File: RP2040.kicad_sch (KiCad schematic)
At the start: 1 part, among them U1 RP2040

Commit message: more rp2040 work
-BMS updates
- rp2040 updates
- add hardware design docs
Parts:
- added C1, C10, C11, C12, C13, C14, C15, C18, C19, C9: 10µF, symbol Device:C_Small
- added C16, C17: 1µF, symbol Device:C_Small
- added R5, R6: 27.4Ω, symbol Device:R_Small
- U1: Hardware Design Docs (none) -> https://datasheets.raspberrypi.com/rp2040/hardware-design-w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
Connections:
- net +3v3-SYS: now also C1.1, C10.1, C11.1, C12.1, C13.1, C14.1, C15.1, C16.1, C9.1
- net GND: now also C1.2, C10.2, C11.2, C12.2, C13.2, C14.2, C15.2, C16.2, C17.1, C18.2, C19.2, C9.2
- net +1V1: now reaches U1.23 (DVDD), U1.50 (DVDD)
- net +1V1: now also U1.45 (VREG_VOUT), C17.2, C18.1, C19.1
- net at U1.46 (USB_DM): now also R6.1
- net at U1.47 (USB_DP): now also R5.2
- net QSPI_SD3: now reaches U1.51 (QSPI_SD3)
- net QSPI_SCLK: now reaches U1.52 (QSPI_SCLK)
- net QSPI_SD0: now reaches U1.53 (QSPI_SD0)
- net QSPI_SD2: now reaches U1.54 (QSPI_SD2)
- net QSPI_SD1: now reaches U1.55 (QSPI_SD1)
- net QSPI_SS: now reaches U1.56 (QSPI_SS)
- net MB_SCL renamed SCL2
- net MB_SDA renamed SDA2
- net SYS_SCL renamed SCL1
- net SYS_SDA renamed SDA1
- new net USB_DM: R6.2
- new net USB_DP: R5.1
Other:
- note added: "1µF close to VREG_IN"
- note added: "1µF close to VREG_VOUT"
- note added: "27.4Ω close to D+/D-"
- moved on the sheet: U1

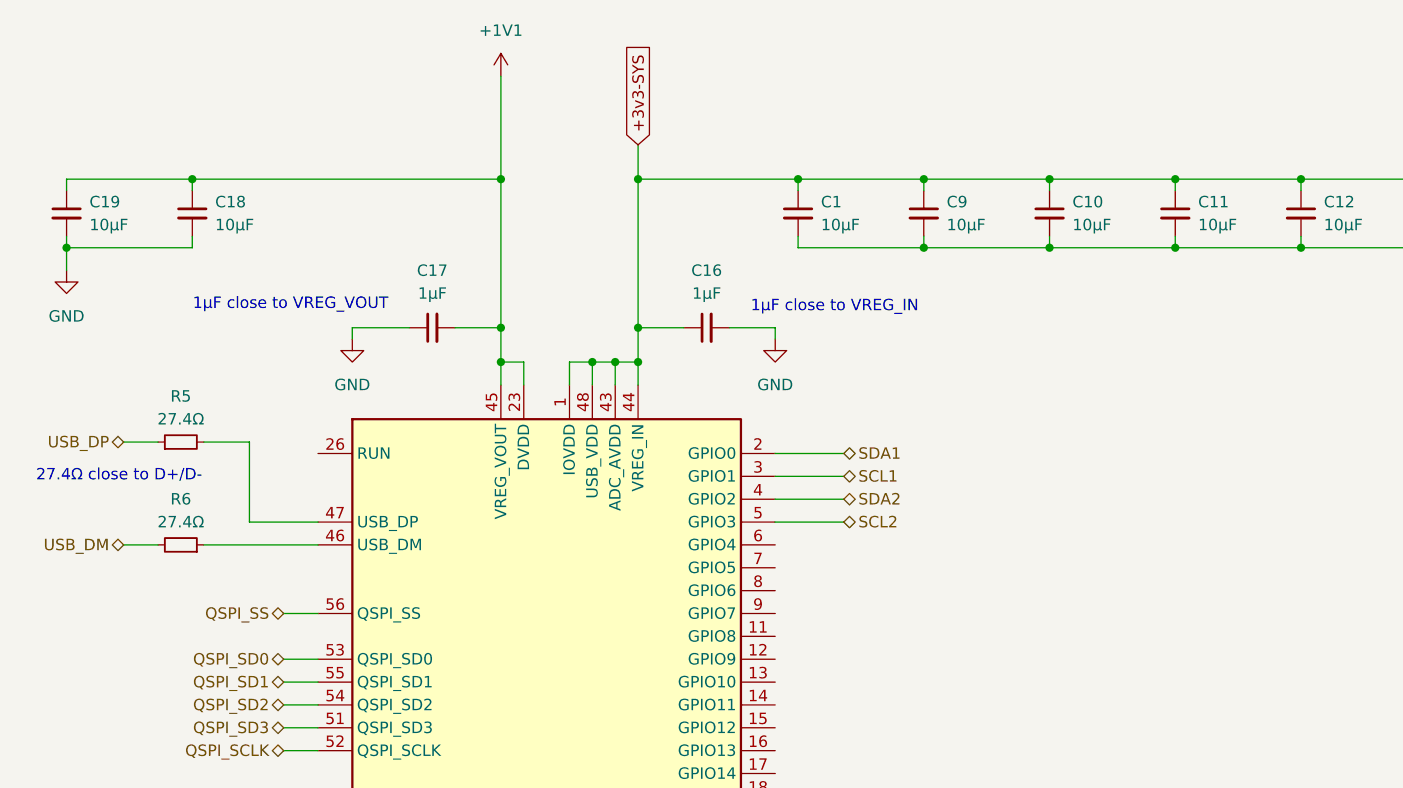
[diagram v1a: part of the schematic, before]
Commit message: BMS updates
- BMS mostly done
- all BMS pins connected to RP2040
- Re-did Minibadge pinouts
- Connected RP2040 to USB Switch
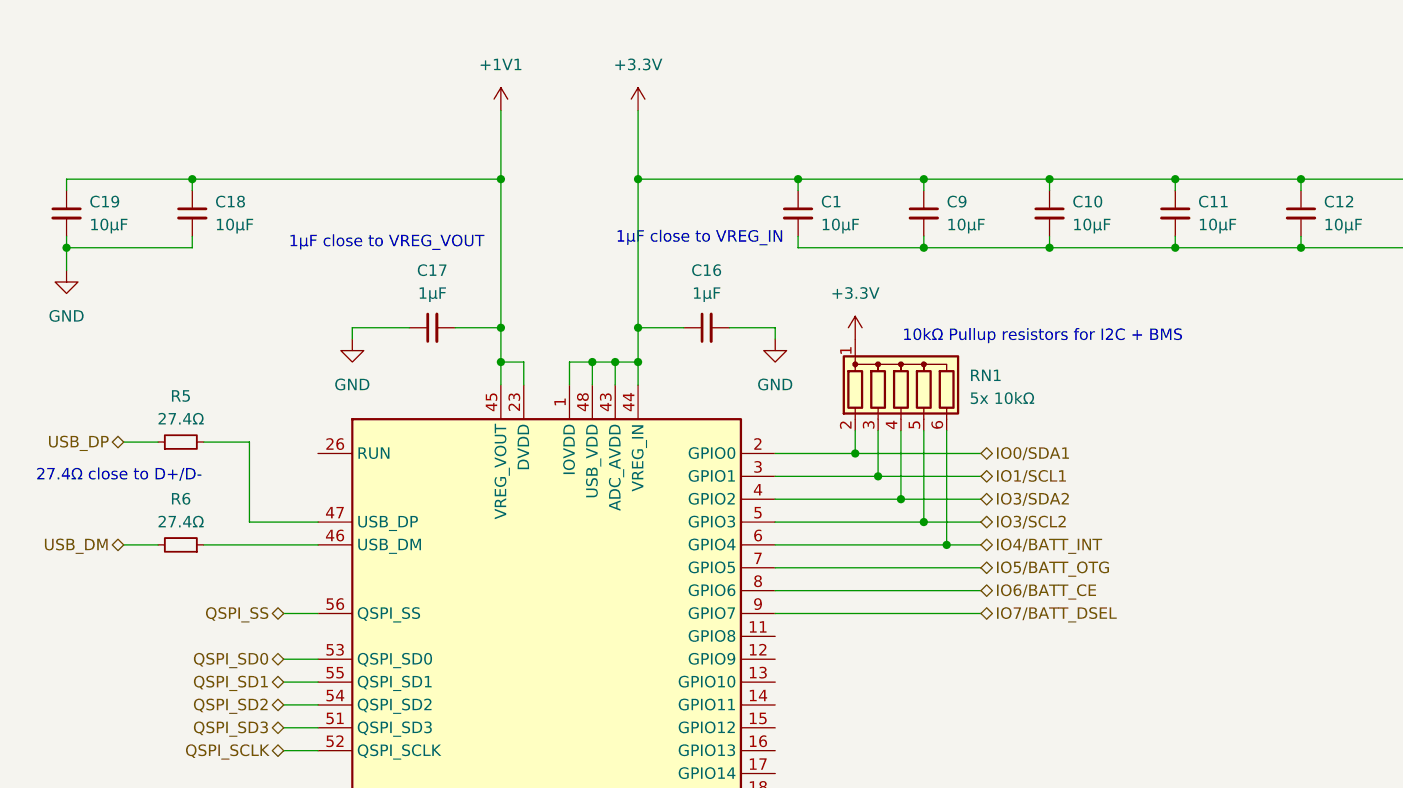
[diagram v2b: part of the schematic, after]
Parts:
- added RN1: 5x 10kΩ, Resistor_THT:R_Array_SIP6, symbol Device:R_Network05
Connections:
- net IO4/BATT_INT: now reaches U1.6 (GPIO4)
- net IO4/BATT_INT: now also RN1.6 (R5)
- net IO5/BATT_OTG: now reaches U1.7 (GPIO5)
- net IO6/BATT_CE: now reaches U1.8 (GPIO6)
- net IO7/BATT_DSEL: now reaches U1.9 (GPIO7)
- net +3v3-SYS renamed +3.3V
- net +3.3V: now also RN1.1 (common)
- net SCL1 renamed IO1/SCL1
- net IO1/SCL1: now also RN1.3 (R2)
- net SCL2 renamed IO3/SCL2
- net IO3/SCL2: now also RN1.5 (R4)
- net SDA1 renamed IO0/SDA1
- net IO0/SDA1: now also RN1.2 (R1)
- net SDA2 renamed IO3/SDA2
- net IO3/SDA2: now also RN1.4 (R3)
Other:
- note added: "10kΩ Pullup resistors for I2C + BMS"
- company: (none) -> Pips Engineering
- title: (none) -> RP2040 MCU

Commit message: cleanup
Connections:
- net IO8/USB_SW_DISABLE: now reaches U1.11 (GPIO8)
- net IO7/BATT_DSEL renamed IO7/USB_SW_DSEL
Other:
- moved on the sheet: RN1
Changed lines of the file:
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@@
 	)
 	(junction
-		(at 140.97 72.39)
-		(diameter 0)
-		(color 0 0 0 0)
-	)
-	(junction
-		(at 151.13 82.55)
+		(at 142.24 72.39)
 		(diameter 0)
 		(color 0 0 0 0)
@@
 	)
 	(junction
-		(at 143.51 74.93)
-		(diameter 0)
-		(color 0 0 0 0)
-	)
-	(junction
 		(at 176.53 49.53)
 		(diameter 0)
@@
 	)
 	(junction
+		(at 147.32 77.47)
+		(diameter 0)
+		(color 0 0 0 0)
+	)
+	(junction
 		(at 232.41 49.53)
 		(diameter 0)
@@
 	)
 	(junction
-		(at 146.05 77.47)
+		(at 152.4 82.55)
+		(diameter 0)
+		(color 0 0 0 0)
+	)
+	(junction
+		(at 149.86 80.01)
 		(diameter 0)
 		(color 0 0 0 0)
@@
 	)
 	(junction
+		(at 144.78 74.93)
+		(diameter 0)
+		(color 0 0 0 0)
+	)
+	(junction
 		(at 162.56 41.91)
 		(diameter 0)
@@
 	)
 	(junction
-		(at 148.59 80.01)
-		(diameter 0)
-		(color 0 0 0 0)
-	)
-	(junction
 		(at 101.6 62.23)
 		(diameter 0)
@@
 	(wire
 		(pts
-			(xy 132.08 82.55) (xy 151.13 82.55)
+			(xy 132.08 82.55) (xy 152.4 82.55)
 		)
 		(stroke
@@
 	(wire
 		(pts
-			(xy 148.59 80.01) (xy 154.94 80.01)
-		)
-		(stroke
-			(width 0)
-			(type default)
-		)
-	)
-	(wire
-		(pts
-			(xy 151.13 82.55) (xy 154.94 82.55)
-		)
-		(stroke
-			(width 0)
-			(type default)
-		)
-	)
-	(wire
-		(pts
 			(xy 232.41 41.91) (xy 218.44 41.91)
 		)
@@
 	(wire
 		(pts
-			(xy 143.51 69.85) (xy 143.51 74.93)
+			(xy 144.78 68.58) (xy 144.78 74.93)
 		)
 		(stroke
@@
 	(wire
 		(pts
+			(xy 132.08 92.71) (xy 154.94 92.71)
+		)
+		(stroke
+			(width 0)
+			(type default)
+		)
+	)
+	(wire
+		(pts
 			(xy 176.53 49.53) (xy 190.5 49.53)
 		)
@@
 	(wire
 		(pts
+			(xy 152.4 82.55) (xy 154.94 82.55)
+		)
+		(stroke
+			(width 0)
+			(type default)
+		)
+	)
+	(wire
+		(pts
 			(xy 218.44 48.26) (xy 218.44 49.53)
 		)
@@
 	(wire
 		(pts
-			(xy 146.05 69.85) (xy 146.05 77.47)
+			(xy 147.32 77.47) (xy 154.94 77.47)
+		)
+		(stroke
+			(width 0)
+			(type default)
+		)
+	)
+	(wire
+		(pts
+			(xy 149.86 80.01) (xy 154.94 80.01)
+		)
+		(stroke
+			(width 0)
+			(type default)
+		)
+	)
+	(wire
+		(pts
+			(xy 147.32 68.58) (xy 147.32 77.47)
 		)
 		(stroke
@@
 	(wire
 		(pts
-			(xy 148.59 69.85) (xy 148.59 80.01)
+			(xy 149.86 68.58) (xy 149.86 80.01)
 		)
 		(stroke
@@
 	(wire
 		(pts
-			(xy 132.08 80.01) (xy 148.59 80.01)
+			(xy 132.08 80.01) (xy 149.86 80.01)
 		)
 		(stroke
@@
 	(wire
 		(pts
-			(xy 146.05 77.47) (xy 154.94 77.47)
-		)
-		(stroke
-			(width 0)
-			(type default)
-		)
-	)
-	(wire
-		(pts
 			(xy 176.53 41.91) (xy 190.5 41.91)
 		)
@@
 	(wire
 		(pts
-			(xy 143.51 74.93) (xy 154.94 74.93)
-		)
-		(stroke
-			(width 0)
-			(type default)
-		)
-	)
-	(wire
-		(pts
 			(xy 190.5 49.53) (xy 204.47 49.53)
 		)
@@
 	(wire
 		(pts
-			(xy 132.08 74.93) (xy 143.51 74.93)
+			(xy 132.08 74.93) (xy 144.78 74.93)
 		)
 		(stroke
@@
 	(wire
 		(pts
-			(xy 132.08 77.47) (xy 146.05 77.47)
+			(xy 132.08 77.47) (xy 147.32 77.47)
 		)
 		(stroke
@@
 	(wire
 		(pts
-			(xy 140.97 72.39) (xy 154.94 72.39)
-		)
-		(stroke
-			(width 0)
-			(type default)
-		)
-	)
-	(wire
-		(pts
 			(xy 77.47 100.33) (xy 81.28 100.33)
 		)
@@
 	(wire
 		(pts
+			(xy 144.78 74.93) (xy 154.94 74.93)
+		)
+		(stroke
+			(width 0)
+			(type default)
+		)
+	)
+	(wire
+		(pts
 			(xy 101.6 62.23) (xy 101.6 64.77)
 		)
@@
 	(wire
 		(pts
-			(xy 140.97 69.85) (xy 140.97 72.39)
+			(xy 142.24 68.58) (xy 142.24 72.39)
 		)
 		(stroke
@@
 	(wire
 		(pts
-			(xy 132.08 72.39) (xy 140.97 72.39)
+			(xy 132.08 72.39) (xy 142.24 72.39)
 		)
 		(stroke
@@
 	(wire
 		(pts
-			(xy 151.13 69.85) (xy 151.13 82.55)
+			(xy 152.4 68.58) (xy 152.4 82.55)
 		)
 		(stroke
@@
 		(pts
 			(xy 116.84 62.23) (xy 116.84 64.77)
+		)
+		(stroke
+			(width 0)
+			(type default)
+		)
+	)
+	(wire
+		(pts
+			(xy 142.24 72.39) (xy 154.94 72.39)
 		)
 		(stroke
@@
 	(text "10kΩ Pullup resistors for I2C + BMS"
 		(exclude_from_sim no)
-		(at 161.798 59.436 0)
+		(at 163.322 58.166 0)
 		(effects
 			(font
@@
 	(text "1µF close to VREG_IN"
 		(exclude_from_sim no)
-		(at 123.698 48.514 0)
+		(at 122.682 49.022 0)
 		(effects
 			(font
@@
 		)
 	)
-	(hierarchical_label "IO7{slash}BATT_DSEL"
+	(hierarchical_label "IO7/USB_SW_DSEL"
 		(shape bidirectional)
 		(at 154.94 90.17 0)
@@
 		(shape bidirectional)
 		(at 154.94 72.39 0)
+		(effects
+			(font
+				(size 1.27 1.27)
+			)
+			(justify left)
+		)
+	)
+	(hierarchical_label "IO8{slash}USB_SW_DISABLE"
+		(shape output)
+		(at 154.94 92.71 0)
 		(effects
 			(font
@@
 	(symbol
 		(lib_id "Device:R_Network05")
-		(at 146.05 64.77 0)
+		(at 147.32 63.5 0)
 		(unit 1)
 		(exclude_from_sim no)
@@
 		(fields_autoplaced yes)
 		(property "Reference" "RN1"
-			(at 153.67 63.7539 0)
+			(at 154.94 62.4839 0)
 			(effects
 				(font
@@
 		)
 		(property "Value" "5x 10kΩ"
-			(at 153.67 66.2939 0)
+			(at 154.94 65.0239 0)
 			(effects
 				(font
@@
 		)
 		(property "Footprint" "Resistor_THT:R_Array_SIP6"
-			(at 155.575 64.77 90)
+			(at 156.845 63.5 90)
 			(effects
 				(font
@@
 		)
 		(property "Datasheet" "http://www.vishay.com/docs/31509/csc.pdf"
-			(at 146.05 64.77 0)
+			(at 147.32 63.5 0)
 			(effects
 				(font
@@
 		)
 		(property "Description" "5 resistor network, star topology, bussed resistors, small symbol"
-			(at 146.05 64.77 0)
+			(at 147.32 63.5 0)
 			(effects
 				(font
@@
 	(symbol
 		(lib_id "power:+3.3V")
-		(at 140.97 59.69 0)
+		(at 142.24 58.42 0)
 		(unit 1)
 		(exclude_from_sim no)
@@
 		(fields_autoplaced yes)
 		(property "Reference" "#PWR0120"
-			(at 140.97 63.5 0)
+			(at 142.24 62.23 0)
 			(effects
 				(font
@@
 		)
 		(property "Value" "+3.3V"
-			(at 140.97 54.61 0)
+			(at 142.24 53.34 0)
 			(effects
 				(font
@@
 		)
 		(property "Footprint" ""
-			(at 140.97 59.69 0)
+			(at 142.24 58.42 0)
 			(effects
 				(font
@@
 		)
 		(property "Datasheet" ""
-			(at 140.97 59.69 0)
+			(at 142.24 58.42 0)
 			(effects
 				(font
@@
 		)
 		(property "Description" "Power symbol creates a global label with name \"+3.3V\""
-			(at 140.97 59.69 0)
-			(effects
-				(font
+			(at 142.24 58.42 0)
+			(effects
+				(font
